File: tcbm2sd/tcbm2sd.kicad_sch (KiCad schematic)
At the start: 13 parts, among them J2 JTAG, J3 debug, J4 AMS1117, J5 SD CARD, J7 debug, J8 C16-Exp-Port, U1 XC9572XL-VQ64, U2 Arduino_Pro_Mini

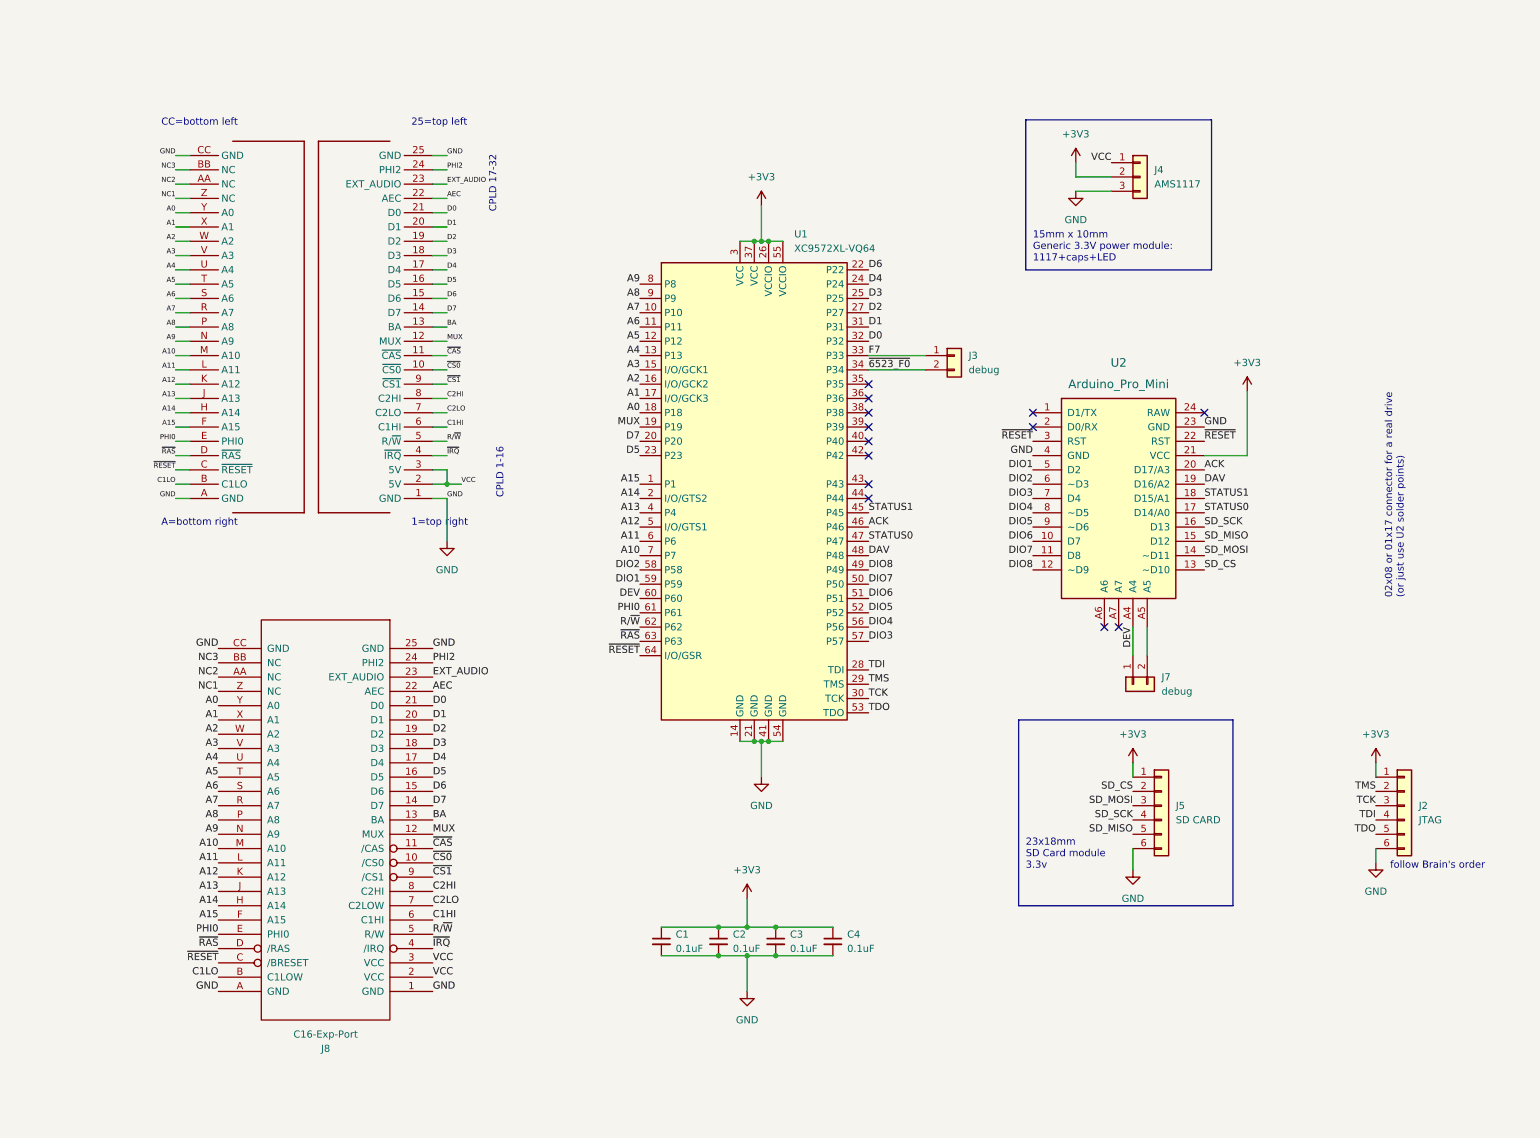
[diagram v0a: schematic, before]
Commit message: update comments, correct central hole size to 5mm
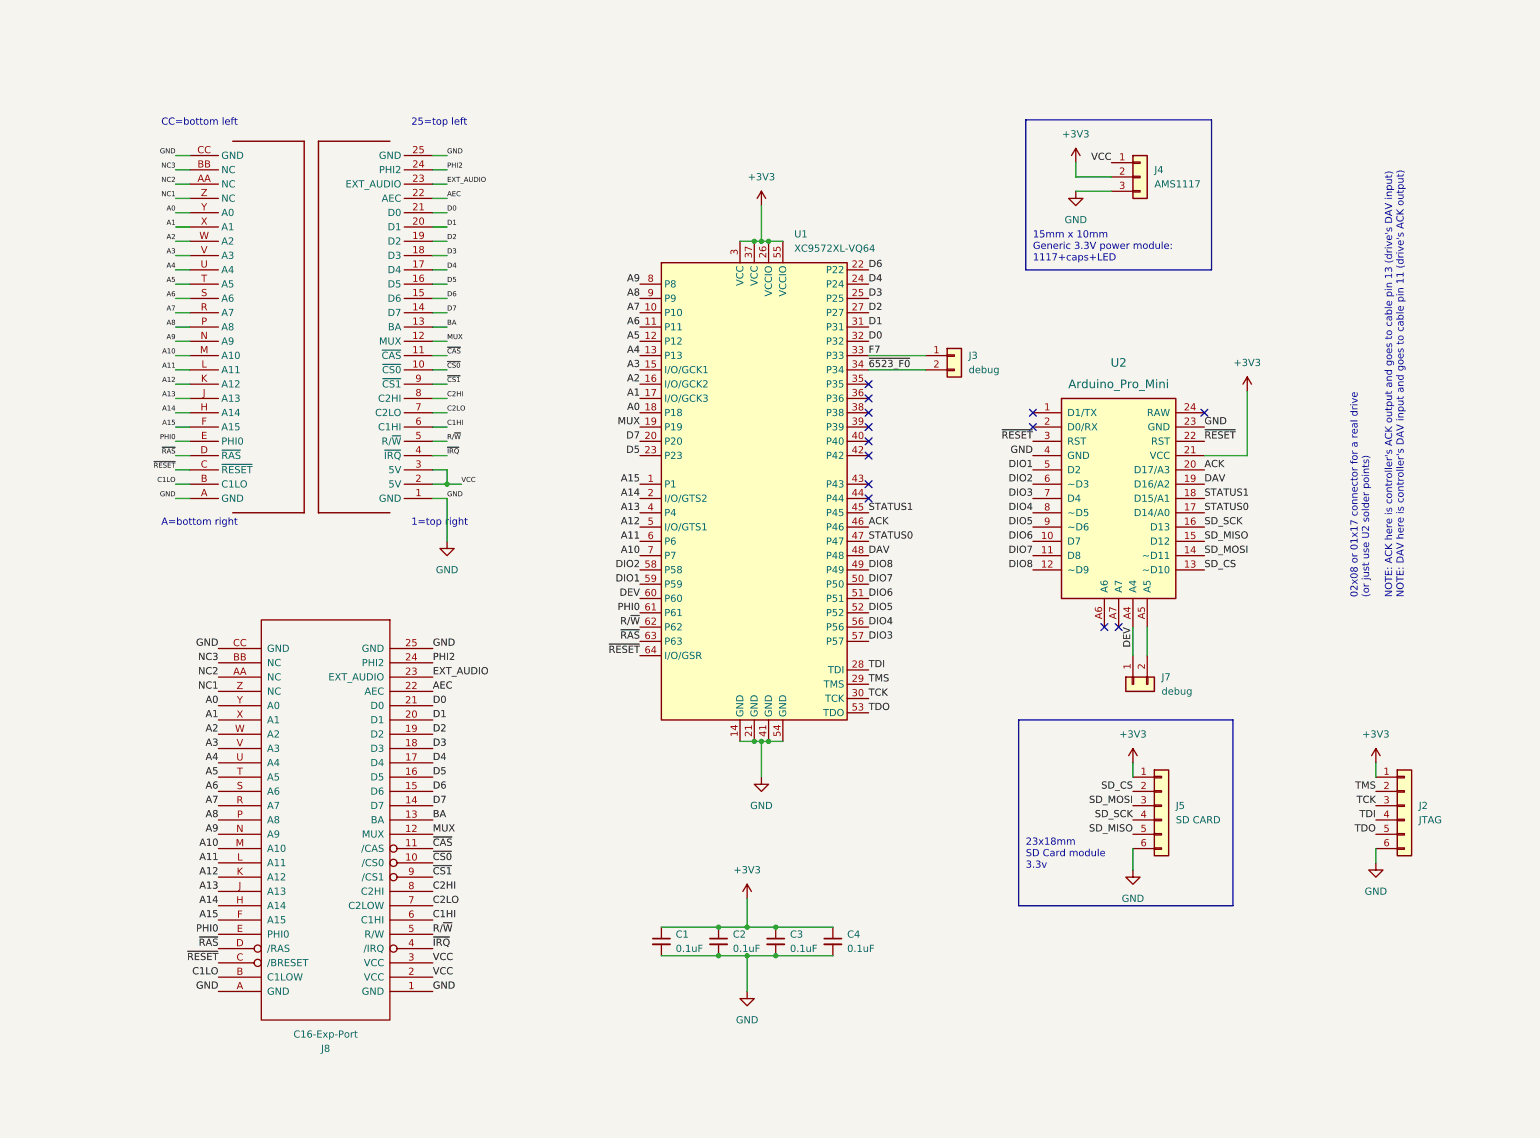
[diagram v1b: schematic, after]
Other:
- note added: "02x08 or 01x17 connector for a real drive (or just use U2 solder points) NOTE: ACK here is controller's ACK output and goes to cable pin 13 (drive's DAV input) NOTE: DAV here is controller's DAV input and goes to cable pin 11 (drive's ACK output)"
- note removed: "02x08 or 01x17 connector for a real drive (or just use U2 solder points)"
- note removed: "CPLD 1-16"
- note removed: "CPLD 17-32"
- note removed: "follow Brain's order"
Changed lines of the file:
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@@
     (effects (font (size 1.27 1.27)) (justify left bottom))
   )
-  (text "follow Brain's order" (at 264.16 149.86 0)
-    (effects (font (size 1.27 1.27)) (justify left bottom))
-  )
-  (text "02x08 or 01x17 connector for a real drive\n(or just use U2 solder points)"
+  (text "02x08 or 01x17 connector for a real drive\n(or just use U2 solder points)\n\nNOTE: ACK here is controller's ACK output and goes to cable pin 13 (drive's DAV input)\nNOTE: DAV here is controller's DAV input and goes to cable pin 11 (drive's ACK output)\n"
     (at 266.7 101.6 90)
     (effects (font (size 1.27 1.27)) (justify left bottom))
@@
     (effects (font (size 1.27 1.27)) (justify left bottom))
   )
-  (text "CPLD 1-16" (at 106.68 83.82 90)
-    (effects (font (size 1.27 1.27)) (justify left bottom))
-  )
-  (text "CPLD 17-32" (at 105.41 33.02 90)
-    (effects (font (size 1.27 1.27)) (justify left bottom))
-  )

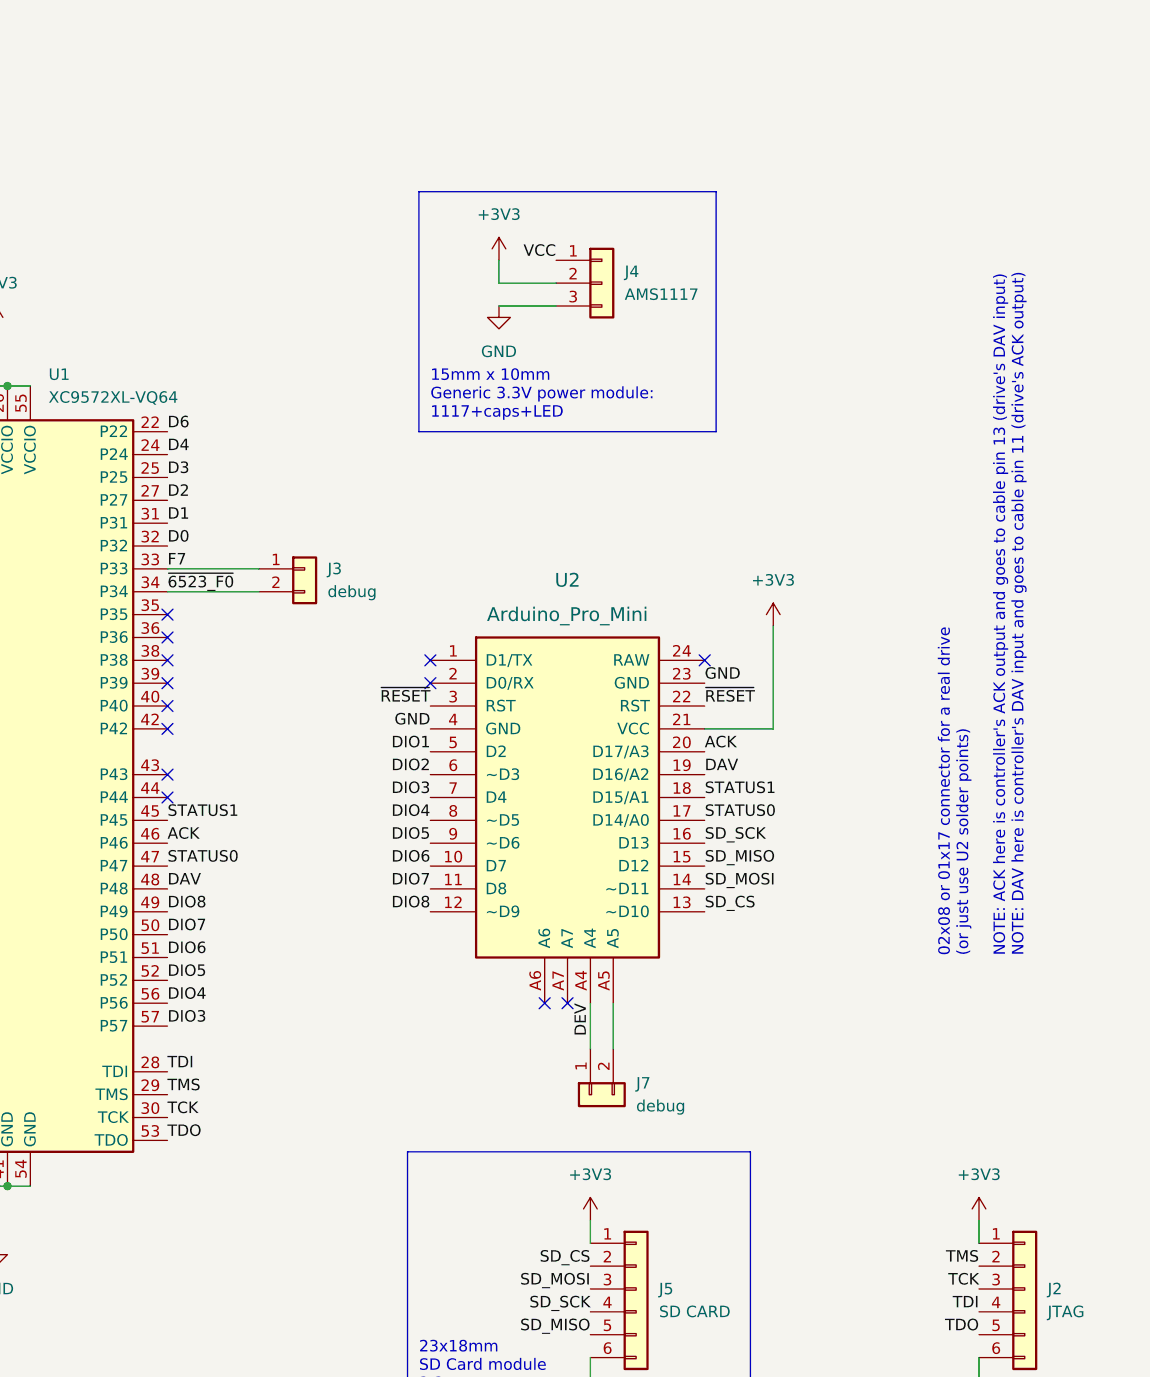
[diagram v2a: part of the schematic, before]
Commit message: - solder jumpers to choose DEV from +33V/GND/A4/D1 - TCBM connector - removed debug pads - RESET 3.3V, through solder jumper - cut connection to Arduino pin 3 (RP2040 clone has GND there) - VCC net class with wider trace
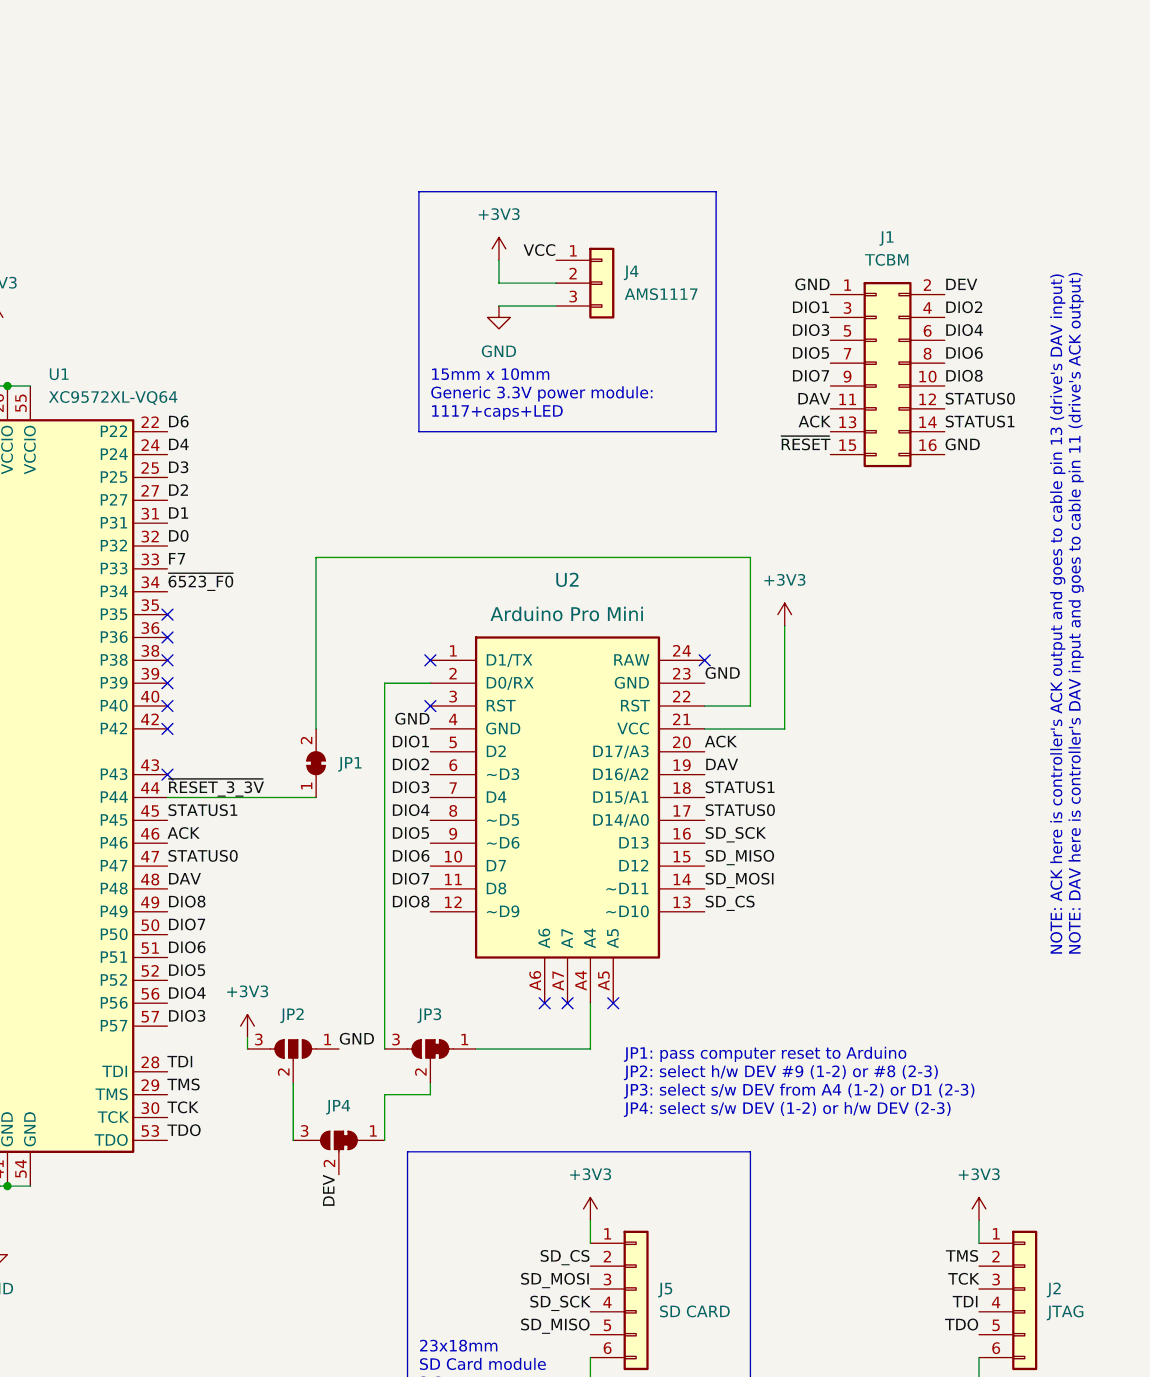
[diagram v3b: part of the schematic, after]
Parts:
- removed J3, J7: debug, Connector_PinHeader_2.54mm:PinHeader_1x02_P2.54mm_Vertical, symbol Connector_Generic:Conn_01x02
- added J1: TCBM, Connector_PinHeader_2.54mm:PinHeader_2x08_P2.54mm_Vertical, symbol Connector_Generic:Conn_02x08_Odd_Even
- added JP1: SolderJumper_2_Bridged, Jumper:SolderJumper-2_P1.3mm_Bridged_Pad1.0x1.5mm, symbol Jumper:SolderJumper_2_Bridged
- added JP2: SolderJumper_3_Open, Jumper:SolderJumper-3_P1.3mm_Open_Pad1.0x1.5mm_NumberLabels, symbol Jumper:SolderJumper_3_Open
- added JP3, JP4: SolderJumper_3_Bridged12, Jumper:SolderJumper-3_P1.3mm_Bridged12_Pad1.0x1.5mm_NumberLabels, symbol Jumper:SolderJumper_3_Bridged12
- U2: value Arduino_Pro_Mini -> Arduino Pro Mini
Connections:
- net +3V3: now also JP2.3 (B)
- net ACK: now also J1.13 (Pin_13)
- net DAV: now also J1.11 (Pin_11)
- net DEV: now also J1.2 (Pin_2), JP4.2 (C); no longer U2.A4
- net DIO1: now also J1.3 (Pin_3)
- net DIO2: now also J1.4 (Pin_4)
- net DIO3: now also J1.5 (Pin_5)
- net DIO4: now also J1.6 (Pin_6)
- net DIO5: now also J1.7 (Pin_7)
- net DIO6: now also J1.8 (Pin_8)
- net DIO7: now also J1.9 (Pin_9)
- net DIO8: now also J1.10 (Pin_10)
- net GND: now also J1.1 (Pin_1), J1.16 (Pin_16), JP2.1 (A)
- net STATUS0: now also J1.12 (Pin_12)
- net STATUS1: now also J1.14 (Pin_14)
- net ~{RESET}: now also J1.15 (Pin_15); no longer U2.22 (RST), U2.3 (RST)
- net at U2.2 (D0/RX): now also JP3.3 (B)
- net ~{RESET_3_3V}: now reaches U1.44 (P44)
- net ~{RESET_3_3V}: now also JP1.1 (A)
- new net: JP2.2 (C), JP4.3 (B)
- new net: JP1.2 (B), U2.22 (RST)
- new net: JP3.1 (A), U2.A4
- new net: JP3.2 (C), JP4.1 (A)
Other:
- note added: "JP1: pass computer reset to Arduino JP2: select h/w DEV #9 (1-2) or #8 (2-3) JP3: select s/w DEV from A4 (1-2) or D1 (2-3) JP4: select s/w DEV (1-2) or h/w DEV (2-3)"
- note added: "NOTE: ACK here is controller's ACK output and goes to cable pin 13 (drive's DAV input) NOTE: DAV here is controller's DAV input and goes to cable pin 11 (drive's ACK output)"
- note removed: "02x08 or 01x17 connector for a real drive (or just use U2 solder points) NOTE: ACK here is controller's ACK output and goes to cable pin 13 (drive's DAV input) NOTE: DAV here is controller's DAV input and goes to cable pin 11 (drive's ACK output)"
